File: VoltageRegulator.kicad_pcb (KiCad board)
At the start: 2 copper layers, 100 x 100 mm, 14 parts, among them J1 Conn_01x02_Female, Q1 VNP10N07

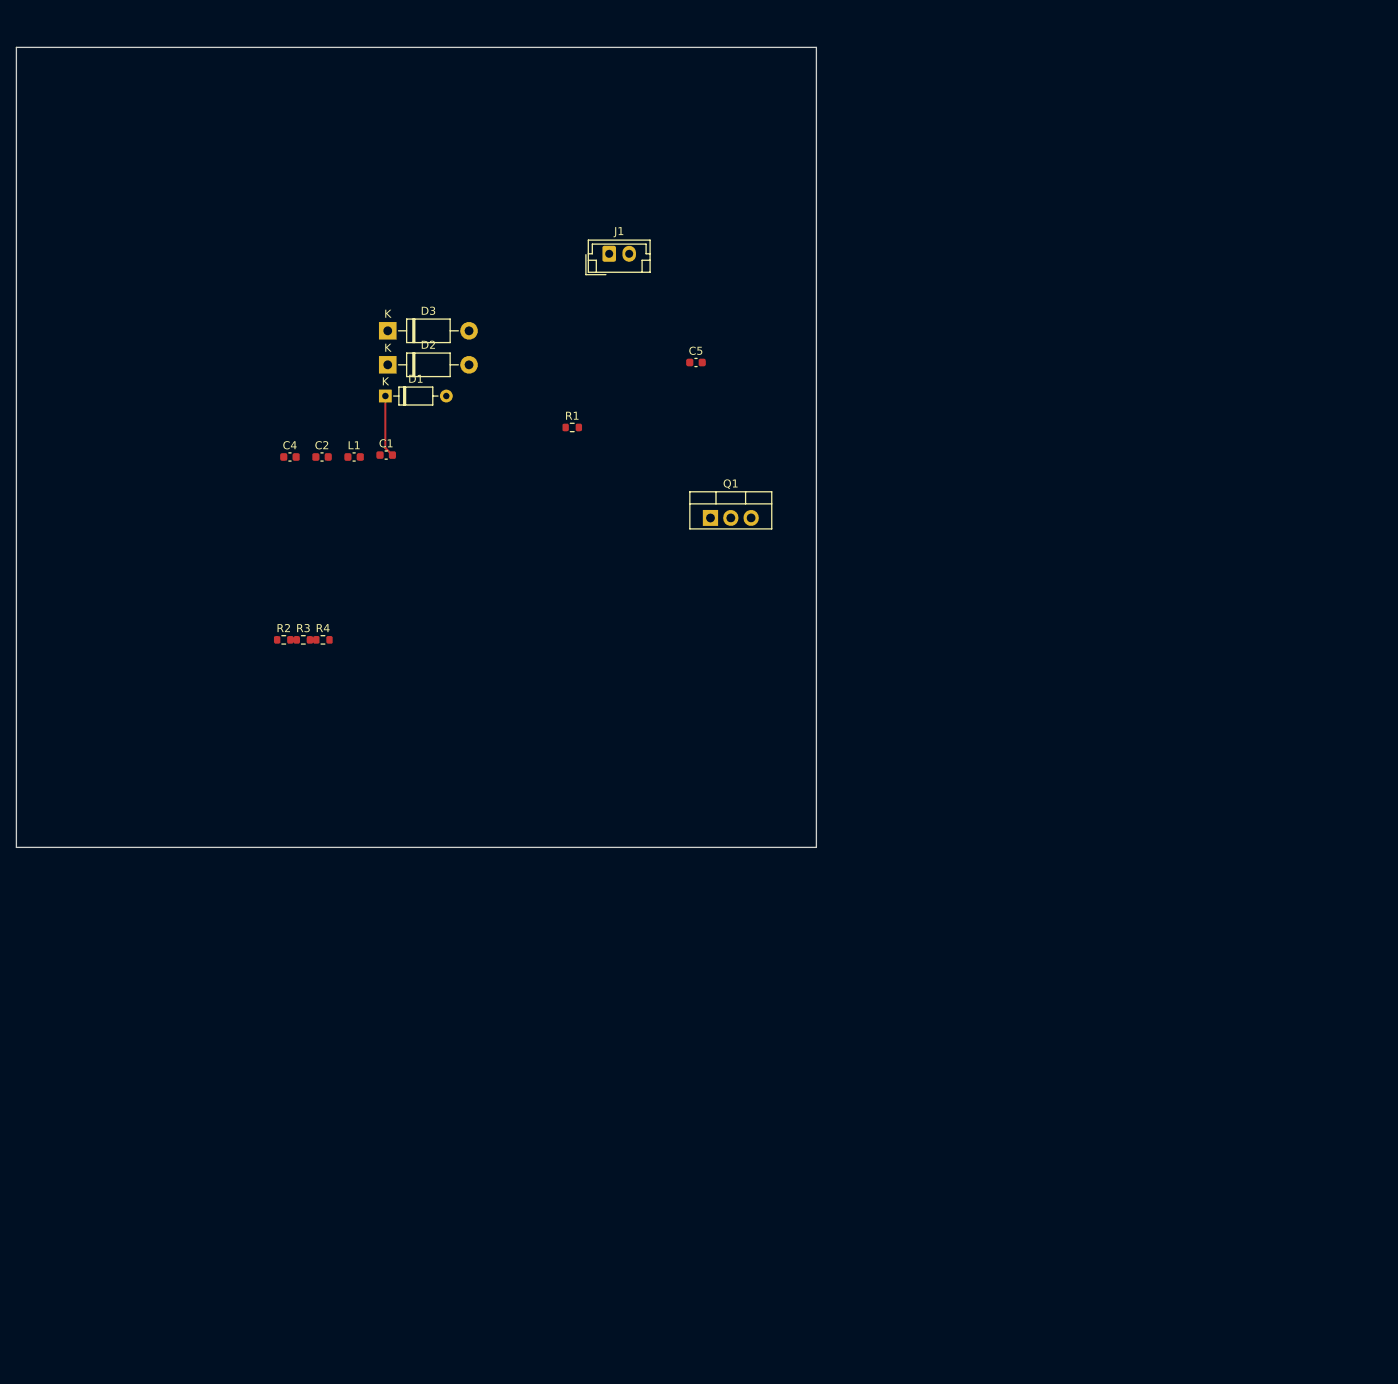
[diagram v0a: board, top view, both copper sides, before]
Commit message: Layout almost finished
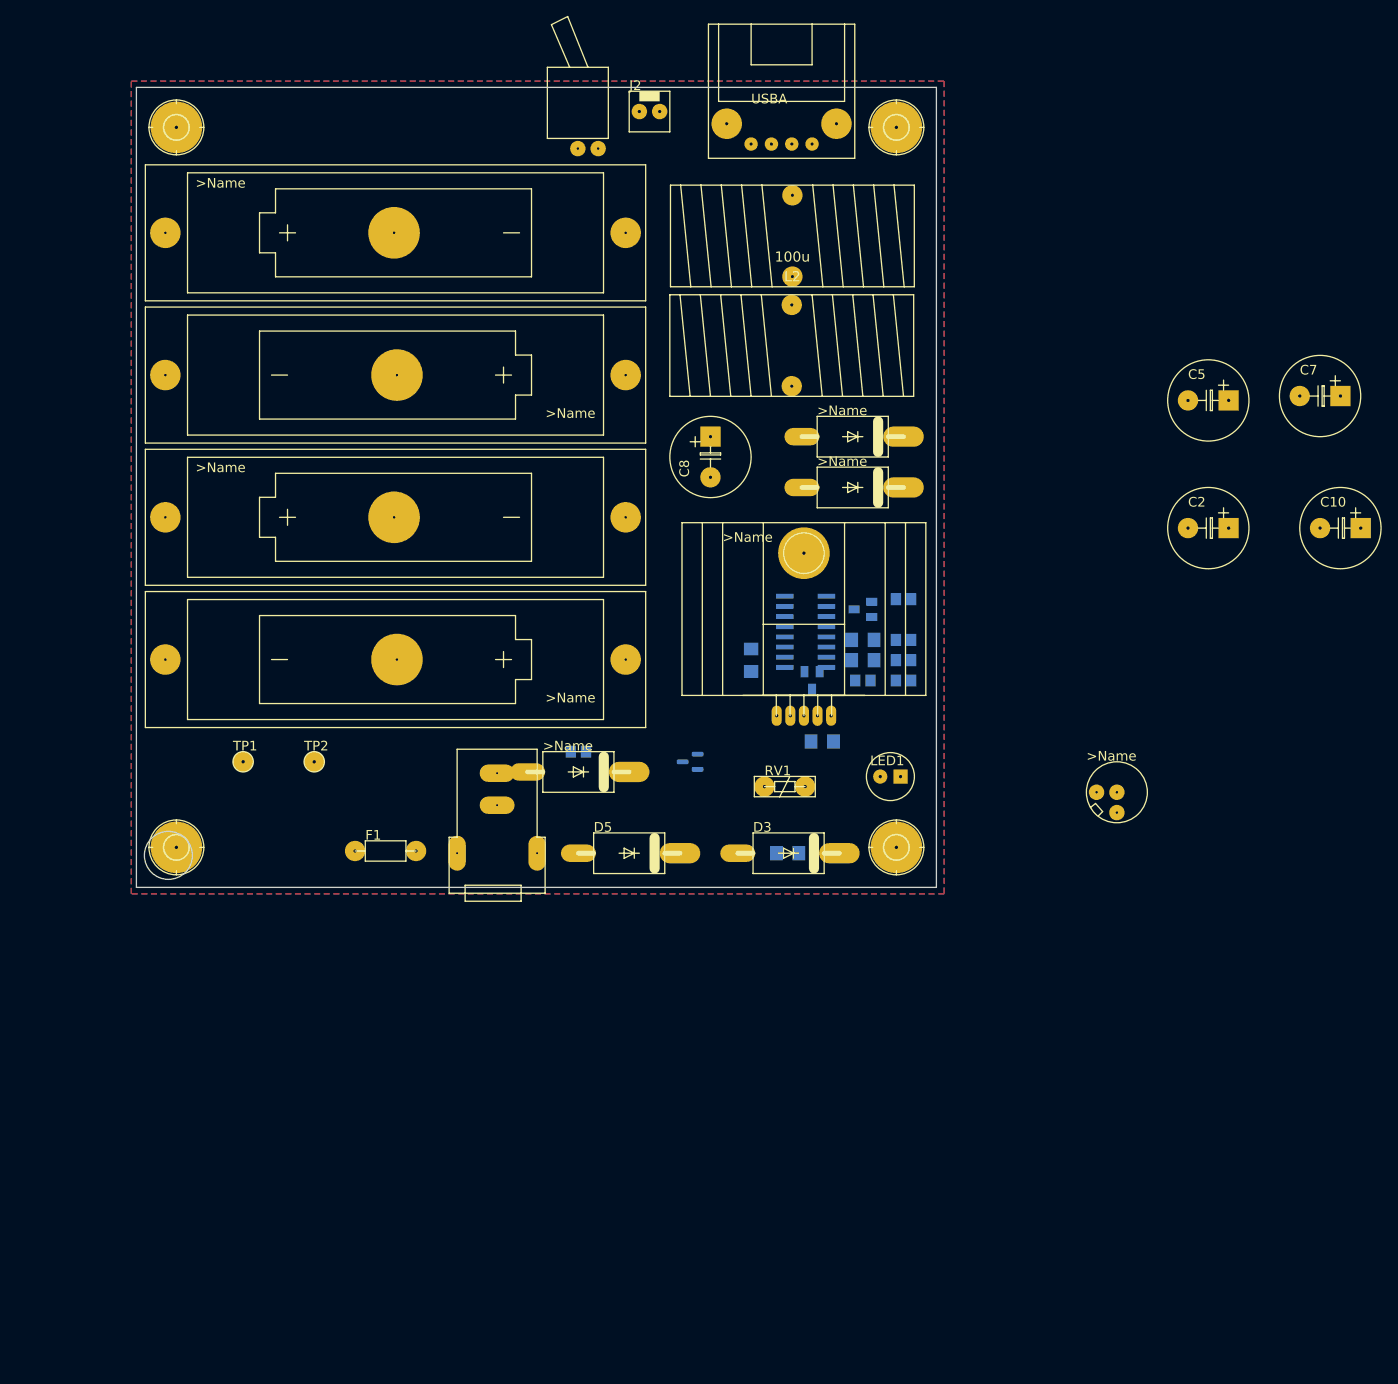
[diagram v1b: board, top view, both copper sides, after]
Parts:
- added BT1: POWER_POWER_AKKU, LIB_Embedsys:POWER_POWER_AKKU_AA, F.Cu at (72.4, 48.2)
- added BT2: POWER_POWER_AKKU, LIB_Embedsys:POWER_POWER_AKKU_AA, F.Cu at (72.4, 66.0)
- added BT3: POWER_POWER_AKKU, LIB_Embedsys:POWER_POWER_AKKU_AA, F.Cu at (72.4, 83.7)
- added BT4: POWER_POWER_AKKU, LIB_Embedsys:POWER_POWER_AKKU_AA, F.Cu at (72.4, 101.5)
- added C10: 470u, LIB_Embedsys:POWER_POWER_C-POL, F.Cu at (190.5, 85.1)
- added C3: 100n, LIB_Embedsys:C1206, B.Cu at (130.8, 99.1)
- added C6: 10n, LIB_Embedsys:C1206, B.Cu at (121.4, 125.7)
- added C7: 330u, LIB_Embedsys:POWER_POWER_C-POL, F.Cu at (188.0, 68.6)
- added C8: 330u, LIB_Embedsys:POWER_POWER_C-POL, F.Cu at (111.8, 76.2)
- added C9: 10n, LIB_Embedsys:C1206, B.Cu at (125.7, 111.8)
- added D4: POWER_POWER_SB560", LIB_Embedsys:POWER_POWER_DO201AD, F.Cu at (95.2, 115.6)
- added D5: POWER_POWER_SB560", LIB_Embedsys:POWER_POWER_DO201AD, F.Cu at (101.6, 125.7)
- added F1: FUSE, LIB_Embedsys:POWER_POWER_DIP2-300R, F.Cu at (71.2, 125.5)
- added H1: MOUNT-PAD-3.0, LIB_Embedsys:POWER_HOLES_3,0-PAD, F.Cu at (45.0, 35.0)
- added H2: MOUNT-PAD-3.0, LIB_Embedsys:POWER_HOLES_3,0-PAD, F.Cu at (45.0, 125.0)
- added H3: MOUNT-PAD-3.0, LIB_Embedsys:POWER_HOLES_3,0-PAD, F.Cu at (135.0, 35.0)
- added H4: MOUNT-PAD-3.0, LIB_Embedsys:POWER_HOLES_3,0-PAD, F.Cu at (135.0, 125.0)
- added J2: PCB Conn, LIB_Embedsys:POWER_POWER_CON2, F.Cu at (104.1, 33.0)
- added J3: General Purpose USB-A, LIB_Embedsys:POWER_POWER_USBA, F.Cu at (124.5, 37.1)
- added L2: 100u, LIB_Embedsys:POWER_POWER_SPULE_STEHEND, F.Cu at (122.0, 53.6)
- added LED1: LED Green, LIB_Embedsys:POWER_POWER_LED-3MM, F.Cu at (134.2, 116.2)
- added Q2: FDN337N, LIB_Embedsys:SOT23, B.Cu at (124.5, 104.1)
- added Q3: Si2319CDS, Package_TO_SOT_SMD:SOT-23, B.Cu at (109.2, 114.3)
- added R5: 10k, LIB_Embedsys:R0805, B.Cu at (95.2, 113.0)
- added R6: 1k, LIB_Embedsys:R0805, B.Cu at (135.9, 104.1)
- added RV1: VDR300, LIB_Embedsys:POWER_POWER_VDR, F.Cu at (121.0, 117.4)
- added SW1: POWER Switch, LIB_Embedsys:POWER_POWER_SWITCH_ON, F.Cu at (96.5, 37.6)
- added TP1: TSTPIN_VCC, LIB_Embedsys:POWER_POWER_TSTPIN, F.Cu at (53.3, 114.3)
- added TP2: TSTPIN_LM2576, LIB_Embedsys:POWER_POWER_TSTPIN, F.Cu at (62.2, 114.3)
- added U1: LT1510CN, LIB_Embedsys:SO16, B.Cu at (123.7, 98.0)
- added U2: LM2576T_ADJ, LIB_Embedsys:POWER_POWER_5_LEAD_TO220, F.Cu at (108.2, 111.1)
- added VR1: 10k, LIB_Embedsys:POWER_POWER_POTI, F.Cu at (162.6, 118.1)
- C1: value 0.22u -> 220n; footprint Capacitor_SMD:C_0603_1608Metric -> LIB_Embedsys:C1206; moved to B.Cu
- C2: value 10u -> 22u; footprint Capacitor_SMD:C_0603_1608Metric -> LIB_Embedsys:POWER_POWER_C-POL
- C4: value 0.1u -> 1u; footprint Capacitor_SMD:C_0603_1608Metric -> LIB_Embedsys:C1206; moved to B.Cu
- C5: value 1u -> 10u; footprint Capacitor_SMD:C_0603_1608Metric -> LIB_Embedsys:POWER_POWER_C-POL
- D1: value 1N914 -> POWER_POWER_SB560"; footprint Diode_THT:D_DO-35_SOD27_P7.62mm_Horizontal -> LIB_Embedsys:POWER_POWER_DO201AD
- D2, D3: value 1N5819 -> POWER_POWER_SB560"; footprint Diode_THT:D_DO-41_SOD81_P10.16mm_Horizontal -> LIB_Embedsys:POWER_POWER_DO201AD
- J1: value Conn_01x02_Female -> POWER_POWER_ROKA-PWR-IN; footprint Connector_JST:JST_EH_B2B-EH-A_1x02_P2.50mm_Vertical -> LIB_Embedsys:POWER_POWER_ROKA-PWR-IN
- L1: footprint Capacitor_SMD:C_0603_1608Metric -> LIB_Embedsys:POWER_POWER_SPULE_STEHEND
- Q1: value VNP10N07 -> FDN337N; footprint Package_TO_SOT_THT:TO-220-3_Vertical -> LIB_Embedsys:SOT23; moved to B.Cu
- R1: value 1k -> 1M; footprint Resistor_SMD:R_0603_1608Metric -> LIB_Embedsys:R0805; moved to B.Cu
- R2: value 300 -> 1k; footprint Resistor_SMD:R_0603_1608Metric -> LIB_Embedsys:R0805; moved to B.Cu
- R3: value 100 -> 1k; footprint Resistor_SMD:R_0603_1608Metric -> LIB_Embedsys:R0805; moved to B.Cu
- R4: value 11k -> 300; footprint Resistor_SMD:R_0603_1608Metric -> LIB_Embedsys:R0805; moved to B.Cu
- moved C2 111.1 mm to (174.0, 85.1)
- moved D3 82.3 mm to (121.5, 125.7)
- moved R2 77.5 mm to (135.9, 99.1), turned to 180 degrees
- moved J1 76.2 mm to (85.1, 125.7)
- moved C4 76.0 mm to (130.8, 101.6), turned to 180 degrees
- moved R3 75.1 mm to (135.9, 101.6), turned to 180 degrees
- moved R4 67.7 mm to (130.8, 104.1), turned to 180 degrees
- moved C5 64.2 mm to (174.0, 69.1)
- moved D1 59.5 mm to (129.5, 80.0)
- moved D2 58.8 mm to (129.5, 73.7)
- moved L1 55.4 mm to (121.9, 67.3)
- moved C1 52.3 mm to (116.8, 101.6), turned to -90 degrees
- moved R1 46.6 mm to (135.9, 94.0), turned to 180 degrees
- moved Q1 22.2 mm to (130.8, 95.2), turned to -90 degrees
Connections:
- C1 pad 1: Net-(1-Pad1) -> /BOOST
- C1 pad 2: Net-(1-Pad2) -> /SW
- C4 pad 1: Net-(1-Pad6) -> Net-(C4-Pad1)
- C4 pad 2: Net-(C4-Pad2) -> /PROG
- L1 pad 1: Net-(1-Pad4) -> /SENSE
- L1 pad 2: Net-(1-Pad1) -> /SW
- Q1 pad 1: unconnected-(Q1-Pad1) -> Net-(Q1-Pad1)
- Q1 pad 2: GND -> unconnected-(Q1-Pad2)
- Q1 pad 3: Net-(Q1-Pad3) -> unconnected-(Q1-Pad3)
- R1 pad 1: Net-(C4-Pad2) -> /VCC
- R1 pad 2: GND -> Net-(Q1-Pad1)
- R2 pad 1: Net-(C5-Pad1) -> GND
- R2 pad 2: GND -> Net-(Q2-Pad1)
- R3 pad 1: Net-(1-Pad7) -> GND
- R3 pad 2: GND -> Net-(C3-Pad1)
- R4 pad 1: Net-(Q1-Pad3) -> GND
- R4 pad 2: Net-(1-Pad7) -> Net-(C4-Pad1)
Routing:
- net Net-(1-Pad2): track 7.74 -> 0.00 mm
- added copper zone on B.Cu, net GND
- added copper zone on F.Cu, net GND
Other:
- outline, holes or cut-outs redrawn

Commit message: Version 1.0
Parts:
- removed BT1, BT2, BT3, BT4: POWER_POWER_AKKU, LIB_Embedsys:POWER_POWER_AKKU_AA
- removed C10: 470u, LIB_Embedsys:POWER_POWER_C-POL
- removed C8: 330u, LIB_Embedsys:POWER_POWER_C-POL
- removed C9: 10n, LIB_Embedsys:C1206
- removed H1, H2, H3, H4: MOUNT-PAD-3.0, LIB_Embedsys:POWER_HOLES_3,0-PAD
- removed J2: PCB Conn, LIB_Embedsys:POWER_POWER_CON2
- removed J3: General Purpose USB-A, LIB_Embedsys:POWER_POWER_USBA
- removed RV1: VDR300, LIB_Embedsys:POWER_POWER_VDR
- removed SW1: POWER Switch, LIB_Embedsys:POWER_POWER_SWITCH_ON
- removed VR1: 10k, LIB_Embedsys:POWER_POWER_POTI
- added AKKU1: 1.2V NIMH, LIB_Embedsys:POWER_POWER_AKKU_AA, F.Cu at (79.2, 98.6)
- added AKKU2: 1.2V NIMH, LIB_Embedsys:POWER_POWER_AKKU_AA, F.Cu at (79.2, 115.8)
- added AKKU3: 1.2V NIMH, LIB_Embedsys:POWER_POWER_AKKU_AA, F.Cu at (79.2, 133.1)
- added AKKU4: 1.2V NIMH, LIB_Embedsys:POWER_POWER_AKKU_AA, F.Cu at (79.2, 150.4)
- added CP1: 330uF-35V, LIB_Embedsys:POWER_POWER_C-POL, F.Cu at (35.6, 139.2)
- added CP2: 330uF-35V, LIB_Embedsys:POWER_POWER_C-POL, F.Cu at (35.8, 155.3)
- added CP3: 330uF-35V, LIB_Embedsys:POWER_POWER_C-POL, F.Cu at (42.6, 147.2)
- added CP4: 330uF/35V, LIB_Embedsys:POWER_POWER_C-POL, F.Cu at (44.0, 162.3)
- added CP5: 10nF, LIB_Embedsys:C1206, B.Cu at (101.5, 165.0)
- added CP6: 470μF/25V4, LIB_Embedsys:POWER_POWER_C-POL, F.Cu at (116.0, 96.3)
- added CP7: 470μF/25V, LIB_Embedsys:POWER_POWER_C-POL, F.Cu at (116.2, 107.3)
- added CP8: 470μF/25V, LIB_Embedsys:POWER_POWER_C-POL, F.Cu at (116.2, 130.2)
- added CP9: 470μF/25V, LIB_Embedsys:POWER_POWER_C-POL, F.Cu at (116.2, 118.7)
- added D6: POWER_POWER_SB560", LIB_Embedsys:POWER_POWER_DO201AD, F.Cu at (126.2, 162.8)
- added D7: 1N4148, LIB_Embedsys:C1206, B.Cu at (121.3, 151.8)
- added D8: 1N4148, LIB_Embedsys:C1206, B.Cu at (125.1, 149.9)
- added D9: ZD8.2V, LIB_Embedsys:C1206, B.Cu at (105.6, 163.6)
- added Q4: SI2369, LIB_Embedsys:SOT23, B.Cu at (122.2, 131.0)
- added R10: 10k, LIB_Embedsys:R0805, B.Cu at (121.9, 149.2)
- added R11: 10k, LIB_Embedsys:R0805, B.Cu at (121.9, 147.0)
- added R12: 1M, LIB_Embedsys:R0805, B.Cu at (121.9, 134.6)
- added R13: 1k, LIB_Embedsys:R0805, B.Cu at (119.7, 102.3)
- added R14: 1M, LIB_Embedsys:R0805, B.Cu at (125.7, 132.1)
- added R15: 1M, LIB_Embedsys:R0805, B.Cu at (125.7, 136.2)
- added R16: 47k, LIB_Embedsys:R0805, B.Cu at (125.7, 140.3)
- added R7: 1M, LIB_Embedsys:R0805, B.Cu at (45.5, 157.1)
- added R8: 0, LIB_Embedsys:R0805, B.Cu at (112.5, 150.4)
- added R9: 390k, LIB_Embedsys:R0805, B.Cu at (125.2, 145.4)
- added S1: LM2576-5T_4V-40V-max3A, LIB_Embedsys:POWER_POWER_TO-220_5_short, F.Cu at (94.6, 163.6)
- added ST1: POWER_POWER_CON2", LIB_Embedsys:POWER_POWER_CON2, F.Cu at (127.0, 108.0)
- added ST2: POWER_POWER_USBA, LIB_Embedsys:POWER_POWER_USBA, F.Cu at (123.2, 124.5)
- added TP10: POWER_POWER_TSTPIN", LIB_Embedsys:POWER_POWER_TSTPIN, F.Cu at (107.7, 159.9)
- added TP11: POWER_POWER_TSTPIN", LIB_Embedsys:POWER_POWER_TSTPIN, F.Cu at (33.8, 175.2)
- added TP3: POWER_POWER_TSTPIN", LIB_Embedsys:POWER_POWER_TSTPIN, F.Cu at (53.9, 170.6)
- added TP4: POWER_POWER_TSTPIN", LIB_Embedsys:POWER_POWER_TSTPIN, F.Cu at (33.9, 167.4)
- added TP5: POWER_POWER_TSTPIN", LIB_Embedsys:POWER_POWER_TSTPIN, F.Cu at (39.9, 175.3)
- added TP6: POWER_POWER_TSTPIN", LIB_Embedsys:POWER_POWER_TSTPIN, F.Cu at (62.0, 160.8)
- added TP7: POWER_POWER_TSTPIN", LIB_Embedsys:POWER_POWER_TSTPIN, F.Cu at (66.0, 160.7)
- added TP8: POWER_POWER_TSTPIN", LIB_Embedsys:POWER_POWER_TSTPIN, F.Cu at (113.0, 183.4)
- added TP9: POWER_POWER_TSTPIN", LIB_Embedsys:POWER_POWER_TSTPIN, F.Cu at (115.6, 143.0)
- added V1: VDR300, LIB_Embedsys:POWER_POWER_VDR, F.Cu at (45.6, 96.0)
- C1: value 220n -> 100nF
- C2: value 22u -> 100nF; footprint LIB_Embedsys:POWER_POWER_C-POL -> LIB_Embedsys:C1206; moved to B.Cu
- C3: value 100n -> 100nF
- C4: value 1u -> 22uF
- C5: value 10u -> 1uF; footprint LIB_Embedsys:POWER_POWER_C-POL -> LIB_Embedsys:C1206; moved to B.Cu
- C6: value 10n -> 100nF
- C7: value 330u -> 100nF; footprint LIB_Embedsys:POWER_POWER_C-POL -> LIB_Embedsys:C1206; moved to B.Cu
- D2: value POWER_POWER_SB560" -> 1N4148; footprint LIB_Embedsys:POWER_POWER_DO201AD -> LIB_Embedsys:C1206; moved to B.Cu
- D5: value POWER_POWER_SB560" -> POWER_POWER_SB560
- F1: value FUSE -> POWER_POWER_FUSE"
- L1: value 33u -> POWER_POWER_SPULE_STEHEND
- L2: value 100u -> POWER_POWER_SPULE_STEHEND
- LED1: value LED Green -> Grün-2,4V-25mA2
- Q2: value FDN337N -> BC848SMD
- Q3: value Si2319CDS -> BC848SMD; footprint Package_TO_SOT_SMD:SOT-23 -> LIB_Embedsys:SOT23
- R1: value 1M -> 100k
- R2: value 1k -> 100k
- R3: value 1k -> 47k
- R4: value 300 -> 330
- R5: value 10k -> 1k
- R6: value 1k -> 10k
- TP1: value TSTPIN_VCC -> POWER_POWER_TSTPIN"
- TP2: value TSTPIN_LM2576 -> POWER_POWER_TSTPIN"
- U2: value LM2576T_ADJ -> POWER_POWER_SWITCH_ON; footprint LIB_Embedsys:POWER_POWER_5_LEAD_TO220 -> LIB_Embedsys:POWER_POWER_SWITCH_ON
- moved C2 151.8 mm to (53.6, 177.5), turned to -90 degrees
- moved C5 147.9 mm to (56.0, 158.2)
- moved L1 132.5 mm to (57.4, 183.1)
- moved D2 130.4 mm to (50.8, 177.5), turned to 90 degrees
- moved R1 115.0 mm to (47.0, 167.0), turned to 90 degrees
- moved R2 114.3 mm to (43.3, 166.1)
- moved L2 106.4 mm to (122.6, 160.0), turned to 90 degrees
- moved R3 104.8 mm to (45.5, 154.6), turned to 0 degrees
- moved D1 103.2 mm to (76.7, 168.7), turned to -90 degrees
- moved Q1 101.3 mm to (49.7, 156.0), turned to 90 degrees
- moved C4 99.1 mm to (50.1, 159.2), turned to 0 degrees
- moved C1 97.1 mm to (56.4, 177.5)
- moved U1 96.4 mm to (54.1, 164.8), turned to 180 degrees
- moved C3 94.8 mm to (62.9, 165.1)
- moved R6 94.7 mm to (56.6, 156.0), turned to 0 degrees
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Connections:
- C1 pad 2: /SW -> Net-(C1-Pad2)
- C3 pad 1: Net-(C3-Pad1) -> GND
- C3 pad 2: /VC -> /VCC
- C4 pad 1: Net-(C4-Pad1) -> GND
- C4 pad 2: /PROG -> BAT
- C6 pad 1: GND -> Net-(C6-Pad1)
- C6 pad 2: /VCC -> GND
- D1 pad A: /SENSE -> GND
- D1 pad K: /BOOST -> Net-(C1-Pad2)
- D3 pad A: /VCC -> Net-(D3-PadA)
- D3 pad K: /VCC -> /+VIN
- D4 pad A: GND -> Net-(D3-PadA)
- D4 pad K: /OUTPUT -> /VCC
- D5 pad A: /OUTPUT -> Net-(D5-PadA)
- F1 pad P$1: /VCC -> Net-(F1-PadP$1)
- F1 pad P$2: Net-(F1-PadP$2) -> Net-(D3-PadA)
- J1 pad +1: Net-(F1-PadP$2) -> Net-(F1-PadP$1)
- J1 pad +2: Net-(F1-PadP$2) -> Net-(F1-PadP$1)
- L1 pad 2: /SW -> Net-(C1-Pad2)
- L2 pad 2: /V_OUT -> Net-(C7-Pad2)
- Q1 pad 2: unconnected-(Q1-Pad2) -> Net-(Q1-Pad2)
- Q1 pad 3: unconnected-(Q1-Pad3) -> BAT
- Q2 pad 2: Net-(Q2-Pad2) -> GND
- Q2 pad 3: /BAT -> Net-(Q2-Pad3)
- Q3 pad 1: /V_OUT -> Net-(Q2-Pad3)
- Q3 pad 2: Net-(Q2-Pad2) -> GND
- Q3 pad 3: /V_OUT -> Net-(Q3-Pad3)
- R1 pad 1: /VCC -> GND
- R1 pad 2: Net-(Q1-Pad1) -> Net-(R1-Pad2)
- R2 pad 1: GND -> Net-(R1-Pad2)
- R2 pad 2: Net-(Q2-Pad1) -> Net-(R2-Pad2)
- R3 pad 1: GND -> Net-(R2-Pad2)
- R3 pad 2: Net-(C3-Pad1) -> Net-(Q1-Pad2)
- R4 pad 1: GND -> Net-(C5-Pad2)
- R4 pad 2: Net-(C4-Pad1) -> GND
- R5 pad 1: GND -> Net-(C6-Pad1)
- R5 pad 2: /PROG -> /VC
- R6 pad 1: Net-(LED1-PadA) -> /PROG
- R6 pad 2: Net-(J2-Pad+5V) -> GND
- TP1 pad P$1: /VCC -> Net-(C1-Pad2)
- TP2 pad P$1: /V_OUT -> Net-(F1-PadP$1)
- U1 pad 11: /BAT -> BAT
- U1 pad 15: unconnected-(U1-Pad15) -> /VCC
- U1 pad 2: /SW -> Net-(C1-Pad2)
- U1 pad 5: unconnected-(U1-Pad5) -> Net-(R1-Pad2)
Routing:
- net Net-(C7-Pad2): track 0.00 -> 112.0 mm, vias 0 -> 2
- net /+VIN: track 0.00 -> 98.6 mm, vias 0 -> 2
- net BAT: track 0.00 -> 89.4 mm
- net /VCC: track 0.00 -> 74.8 mm
- net Net-(C1-Pad2): track 0.00 -> 40.6 mm
- net /SENSE: track 0.00 -> 33.3 mm
- net Net-(D3-PadA): track 0.00 -> 30.9 mm
- net /VC: track 0.00 -> 29.5 mm, vias 0 -> 2
- net Net-(D5-PadA): track 0.00 -> 28.7 mm
- net Net-(D7-Pad1): track 0.00 -> 28.1 mm
- net Net-(D9-Pad1): track 0.00 -> 24.5 mm, vias 0 -> 2
- net Net-(D5-PadK): track 0.00 -> 23.6 mm
- net /BOOST: track 0.00 -> 20.9 mm
- net Net-(F1-PadP$1): track 0.00 -> 19.2 mm
- net Net-(AKKU2-Pad+): track 0.00 -> 17.3 mm
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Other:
- outline, holes or cut-outs redrawn
- board text added: "DC-Voltage-Regulator"
- board text added: "Lötseite"
- board text added: "Marco Dittmann 19.7.2022"
